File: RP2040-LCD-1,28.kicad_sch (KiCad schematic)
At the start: 6 parts, among them J1 Conn_01x03, J2 Conn_01x03, J3 Conn_02x10_Odd_Even, J4 Conn_02x10_Odd_Even

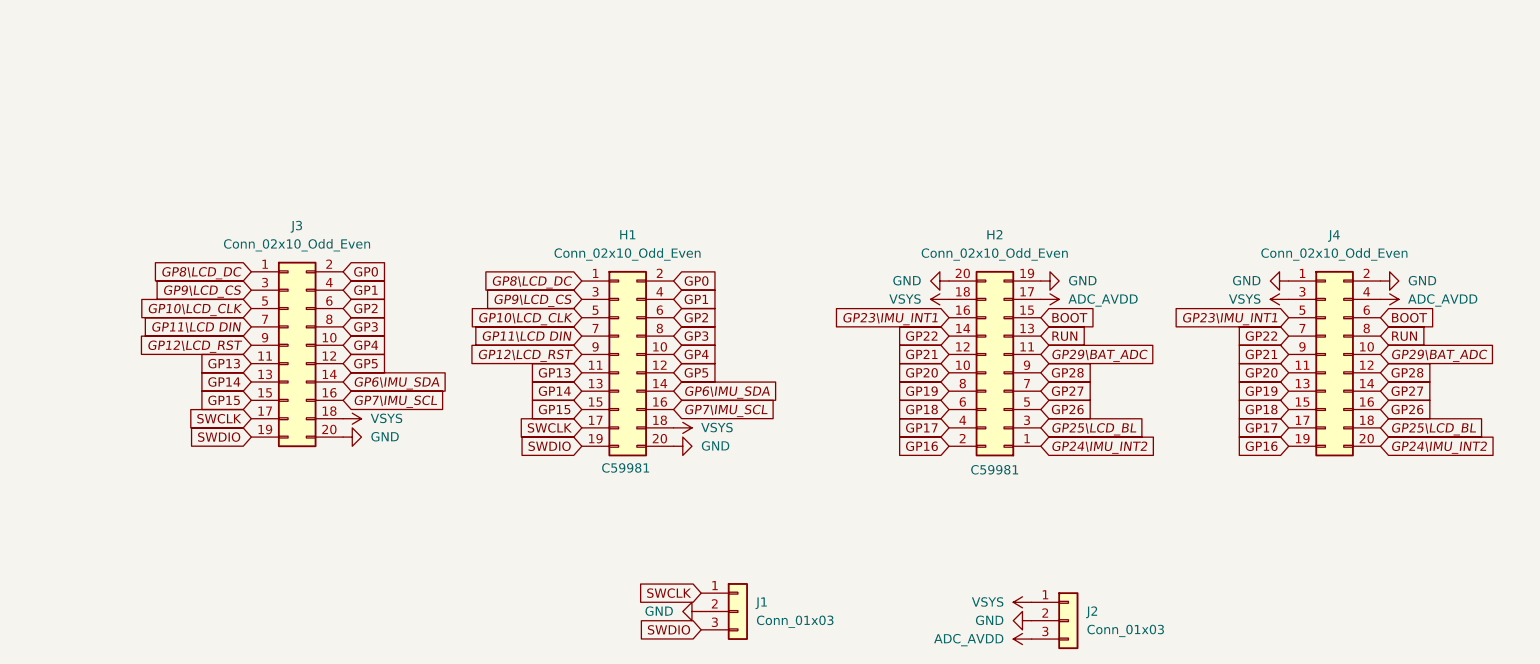
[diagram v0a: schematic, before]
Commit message: Serial Connector added
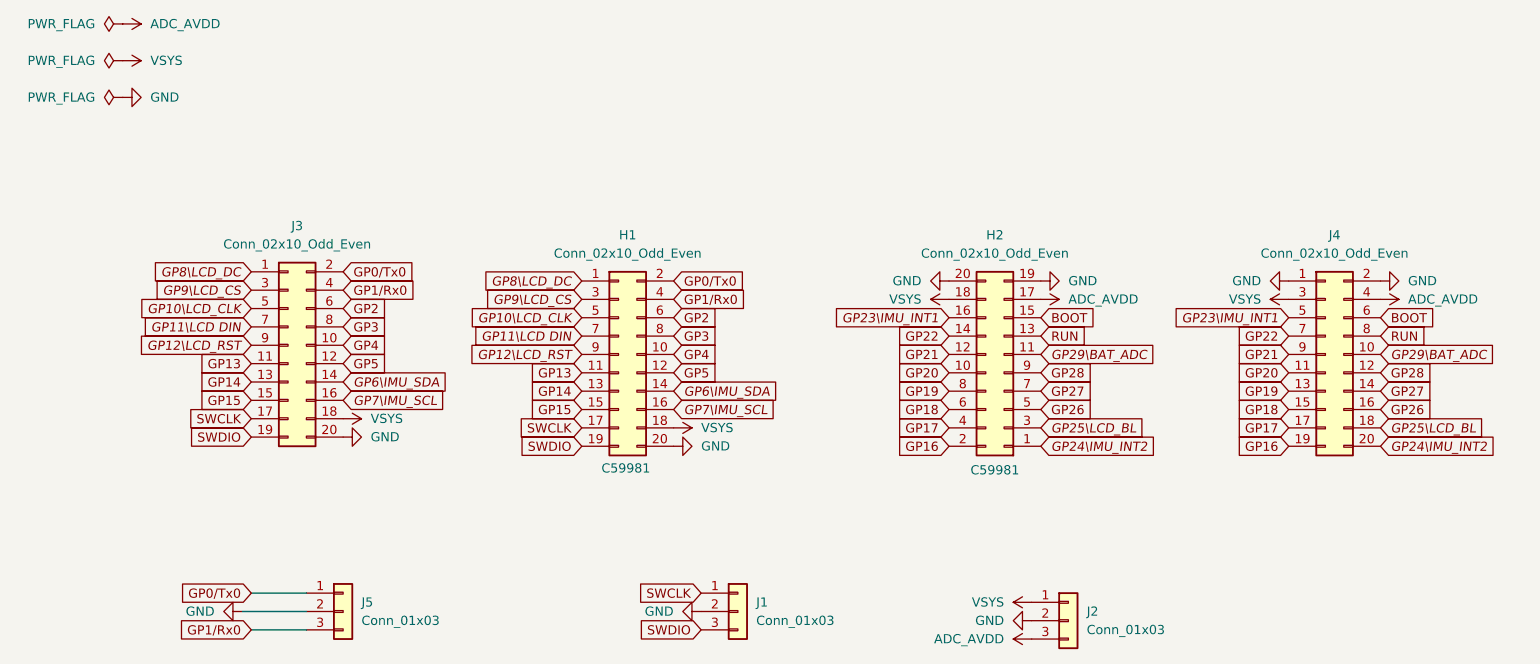
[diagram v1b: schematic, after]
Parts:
- added J5: Conn_01x03, Library:PinHeader_1x03_P2.54mm_Vertical, symbol Connector_Generic:Conn_01x03
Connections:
- net GND: now also J5.2 (Pin_2)
- net GP0 renamed GP0/Tx0
- net GP0/Tx0: now also J5.1 (Pin_1)
- net GP1 renamed GP1/Rx0
- net GP1/Rx0: now also J5.3 (Pin_3)
